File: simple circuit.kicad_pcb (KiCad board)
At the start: 2 copper layers, 49 x 29 mm, 3 parts

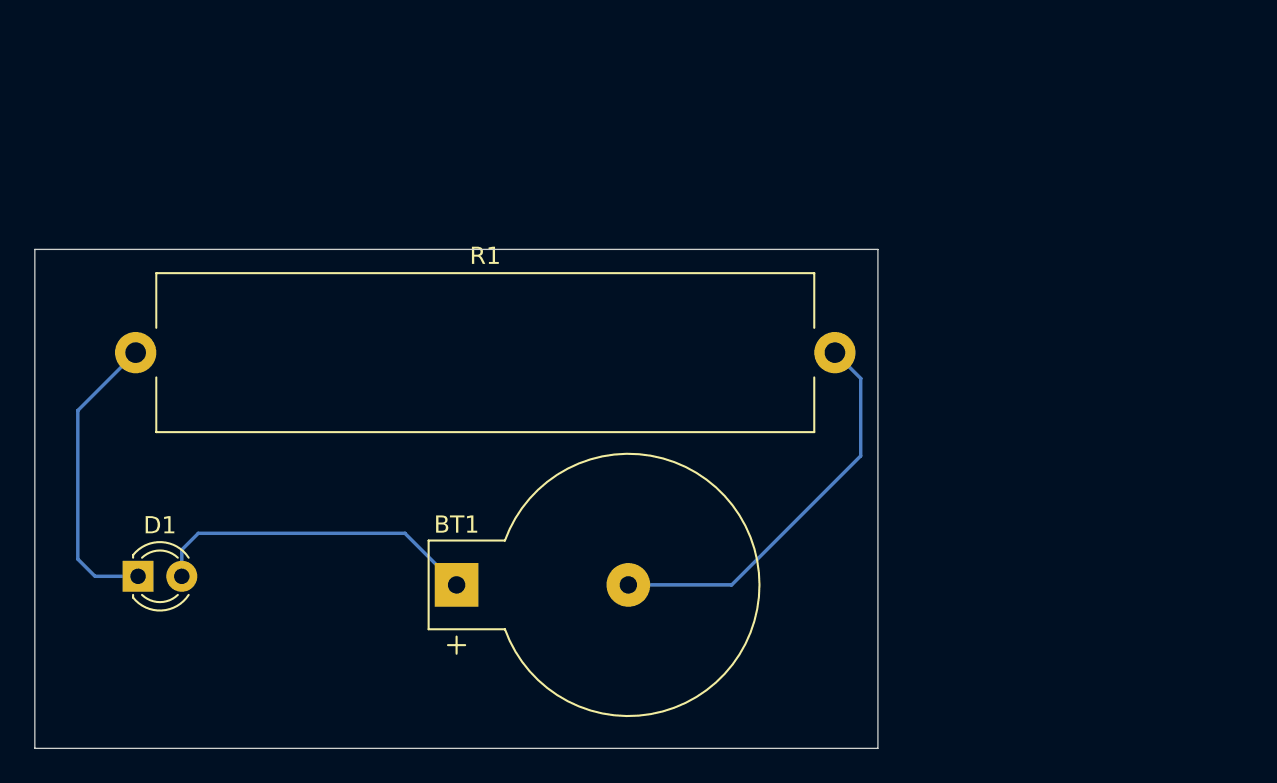
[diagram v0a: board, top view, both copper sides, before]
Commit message: 2 battery and 2 led circuite
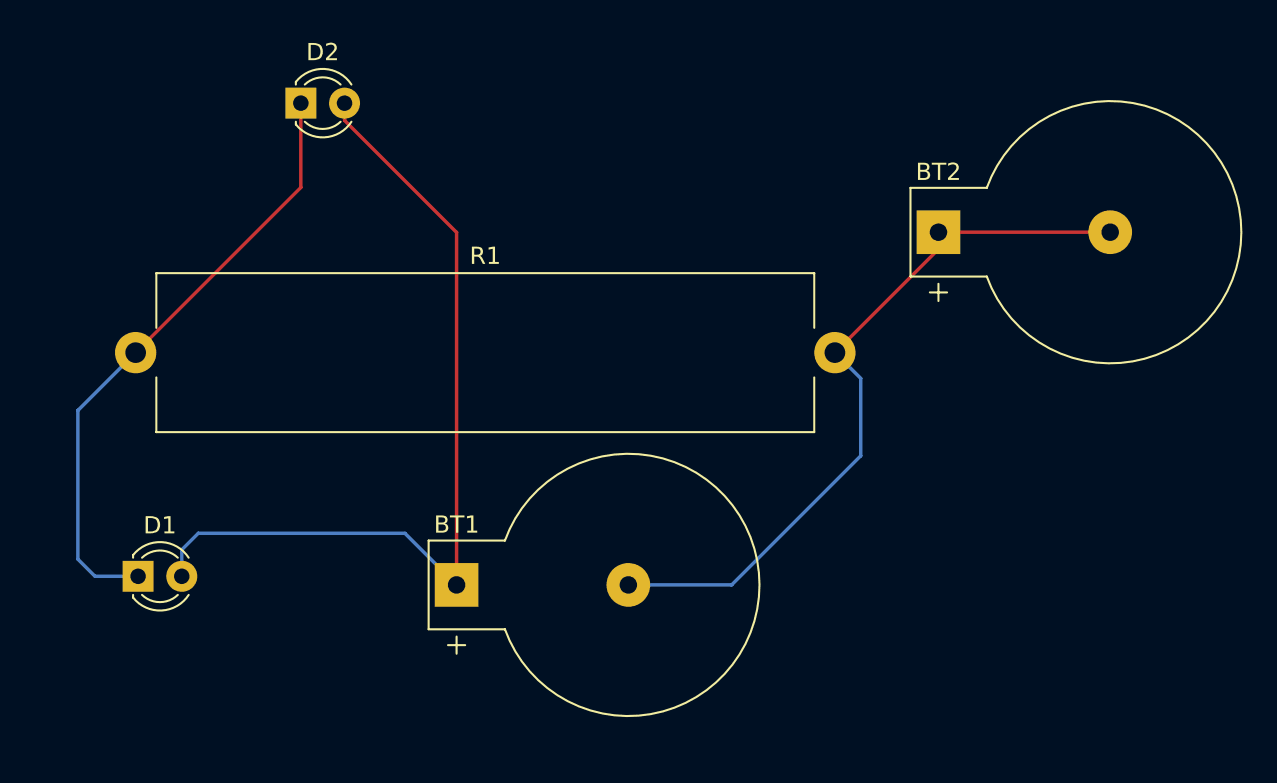
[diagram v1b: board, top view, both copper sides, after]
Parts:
- added BT2: Battery, Battery:BatteryHolder_Keystone_500, F.Cu at (150.5, 82.0)
- added D2: LED, LED_THT:LED_D3.0mm, F.Cu at (113.5, 74.5)
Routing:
- net Net-(BT1-+): track 19.2 -> 49.8 mm
- net Net-(BT1--): track 23.2 -> 42.7 mm
- net Net-(D1-K): track 17.3 -> 35.8 mm
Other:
- board outline removed
